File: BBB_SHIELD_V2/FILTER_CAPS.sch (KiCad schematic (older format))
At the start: 4 parts

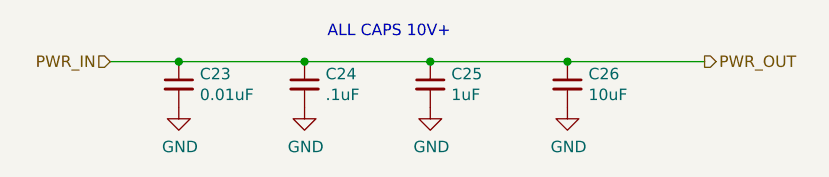
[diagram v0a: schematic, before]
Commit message: Changed to high-side switching of power supply to boards.  Changed footprints to SOIC.  Misc other changes.
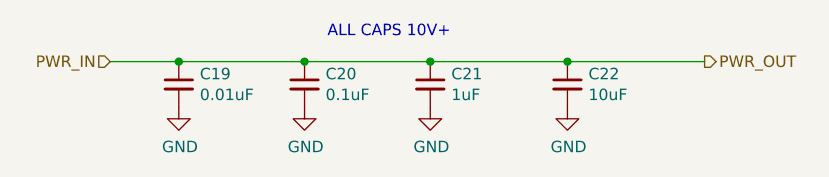
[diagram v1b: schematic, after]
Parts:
- C10: renamed from C18; DKPN (none) -> 1276-1052-1-ND; MFG (none) -> SAMSUNG; MFGPN (none) -> CL21A106KPFNNNE; NOTES (none) -> CT, VER 2018-12-09; TEMPCO (none) -> X5R; VOLTAGE (none) -> 10
- C7: renamed from C15; DKPN (none) -> 1276-1015-1-ND; MFG (none) -> SAMSUNG; MFGPN (none) -> CL21B103KBANNNC; NOTES (none) -> CT, VER 2018-11-25; TEMPCO (none) -> X7R; VOLTAGE (none) -> 50
- C8: renamed from C16; value .1uF -> 0.1uF; DKPN (none) -> 1276-1003-1-ND; MFG (none) -> SAMSUNG; MFGPN (none) -> CL21B104KBCNNNC; NOTES (none) -> REEL, VER 2018-11-25; TEMPCO (none) -> X7R; VOLTAGE (none) -> 50
- C9: renamed from C17; DKPN (none) -> 1276-2928-2-ND; MFG (none) -> SAMSUNG; MFGPN (none) -> CL21B105KBFNFNE; NOTES (none) -> REEL, VER 2018-11-25; TEMPCO (none) -> X7R; VOLTAGE (none) -> 50
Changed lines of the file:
@@
 $Descr A4 11693 8268
 encoding utf-8
-Sheet 7 11
+Sheet 9 12
 Title ""
 Date ""
@@
 PWR_OUT
 $Comp
-L Device:C_Small C15
+L Device:C_Small C7
 U 1 1 5B9ED5AB
 P 3400 2350
-AR Path="/5B9EA430/5B9ED537/5B9ED5AB" Ref="C15"  Part="1"
-AR Path="/5B9EA430/5B9F0FF8/5B9ED5AB" Ref="C19"  Part="1"
-AR Path="/5BA13116/5BD6D0DF/5B9ED5AB" Ref="C23"  Part="1"
-F 0 "C23" H 3492 2396 50  0000 L CNN
+AR Path="/5B9EA430/5B9ED537/5B9ED5AB" Ref="C7"  Part="1"
+AR Path="/5B9EA430/5B9F0FF8/5B9ED5AB" Ref="C11"  Part="1"
+AR Path="/5BA13116/5BD6D0DF/5B9ED5AB" Ref="C?"  Part="1"
+AR Path="/5BA13116/5D116931/5B9ED5AB" Ref="C15"  Part="1"
+AR Path="/5BA13116/5D1169A0/5B9ED5AB" Ref="C19"  Part="1"
+F 0 "C19" H 3492 2396 50  0000 L CNN
 F 1 "0.01uF" H 3492 2305 50  0000 L CNN
 F 2 "Capacitor_SMD:C_0805_2012Metric" H 3400 2350 50  0001 C CNN
-F 3 "~" H 3400 2350 50  0001 C CNN
+F 3 "" H 3400 2350 50  0001 C CNN
+F 4 "1276-1015-1-ND " H 0   0   50  0001 C CNN "DKPN"
+F 5 "SAMSUNG" H 0   0   50  0001 C CNN "MFG"
+F 6 "CL21B103KBANNNC" H 0   0   50  0001 C CNN "MFGPN"
+F 7 "CT, VER 2018-11-25" H 0   0   50  0001 C CNN "NOTES"
+F 8 "X7R" H 0   0   50  0001 C CNN "TEMPCO"
+F 9 "50" H 0   0   50  0001 C CNN "VOLTAGE"
 	1    3400 2350
 	1    0    0    -1
 $EndComp
 $Comp
-L Device:C_Small C16
+L Device:C_Small C8
 U 1 1 5B9ED653
 P 3950 2350
-AR Path="/5B9EA430/5B9ED537/5B9ED653" Ref="C16"  Part="1"
-AR Path="/5B9EA430/5B9F0FF8/5B9ED653" Ref="C20"  Part="1"
-AR Path="/5BA13116/5BD6D0DF/5B9ED653" Ref="C24"  Part="1"
-F 0 "C24" H 4042 2396 50  0000 L CNN
-F 1 ".1uF" H 4042 2305 50  0000 L CNN
+AR Path="/5B9EA430/5B9ED537/5B9ED653" Ref="C8"  Part="1"
+AR Path="/5B9EA430/5B9F0FF8/5B9ED653" Ref="C12"  Part="1"
+AR Path="/5BA13116/5BD6D0DF/5B9ED653" Ref="C?"  Part="1"
+AR Path="/5BA13116/5D116931/5B9ED653" Ref="C16"  Part="1"
+AR Path="/5BA13116/5D1169A0/5B9ED653" Ref="C20"  Part="1"
+F 0 "C20" H 4042 2396 50  0000 L CNN
+F 1 "0.1uF" H 4042 2305 50  0000 L CNN
 F 2 "Capacitor_SMD:C_0805_2012Metric" H 3950 2350 50  0001 C CNN
-F 3 "~" H 3950 2350 50  0001 C CNN
+F 3 "" H 3950 2350 50  0001 C CNN
+F 4 "1276-1003-1-ND " H 0   0   50  0001 C CNN "DKPN"
+F 5 "SAMSUNG" H 0   0   50  0001 C CNN "MFG"
+F 6 "CL21B104KBCNNNC" H 0   0   50  0001 C CNN "MFGPN"
+F 7 "X7R" H 0   0   50  0001 C CNN "TEMPCO"
+F 8 "50" H 0   0   50  0001 C CNN "VOLTAGE"
+F 9 "REEL, VER 2018-11-25" H 0   0   50  0001 C CNN "NOTES"
 	1    3950 2350
 	1    0    0    -1
 $EndComp
 $Comp
-L Device:C_Small C17
+L Device:C_Small C9
 U 1 1 5B9ED6C9
 P 4500 2350
-AR Path="/5B9EA430/5B9ED537/5B9ED6C9" Ref="C17"  Part="1"
-AR Path="/5B9EA430/5B9F0FF8/5B9ED6C9" Ref="C21"  Part="1"
-AR Path="/5BA13116/5BD6D0DF/5B9ED6C9" Ref="C25"  Part="1"
-F 0 "C25" H 4592 2396 50  0000 L CNN
+AR Path="/5B9EA430/5B9ED537/5B9ED6C9" Ref="C9"  Part="1"
+AR Path="/5B9EA430/5B9F0FF8/5B9ED6C9" Ref="C13"  Part="1"
+AR Path="/5BA13116/5BD6D0DF/5B9ED6C9" Ref="C?"  Part="1"
+AR Path="/5BA13116/5D116931/5B9ED6C9" Ref="C17"  Part="1"
+AR Path="/5BA13116/5D1169A0/5B9ED6C9" Ref="C21"  Part="1"
+F 0 "C21" H 4592 2396 50  0000 L CNN
 F 1 "1uF" H 4592 2305 50  0000 L CNN
 F 2 "Capacitor_SMD:C_0805_2012Metric" H 4500 2350 50  0001 C CNN
-F 3 "~" H 4500 2350 50  0001 C CNN
+F 3 "" H 4500 2350 50  0001 C CNN
+F 4 " 1276-2928-2-ND " H 0   0   50  0001 C CNN "DKPN"
+F 5 "SAMSUNG" H 0   0   50  0001 C CNN "MFG"
+F 6 "CL21B105KBFNFNE" H 0   0   50  0001 C CNN "MFGPN"
+F 7 "X7R" H 0   0   50  0001 C CNN "TEMPCO"
+F 8 "50" H 0   0   50  0001 C CNN "VOLTAGE"
+F 9 "REEL, VER 2018-11-25" H 0   0   50  0001 C CNN "NOTES"
 	1    4500 2350
 	1    0    0    -1
 $EndComp
 $Comp
-L Device:C_Small C18
+L Device:C_Small C10
 U 1 1 5B9ED7ED
 P 5100 2350
-AR Path="/5B9EA430/5B9ED537/5B9ED7ED" Ref="C18"  Part="1"
-AR Path="/5B9EA430/5B9F0FF8/5B9ED7ED" Ref="C22"  Part="1"
-AR Path="/5BA13116/5BD6D0DF/5B9ED7ED" Ref="C26"  Part="1"
-F 0 "C26" H 5192 2396 50  0000 L CNN
+AR Path="/5B9EA430/5B9ED537/5B9ED7ED" Ref="C10"  Part="1"
+AR Path="/5B9EA430/5B9F0FF8/5B9ED7ED" Ref="C14"  Part="1"
+AR Path="/5BA13116/5BD6D0DF/5B9ED7ED" Ref="C?"  Part="1"
+AR Path="/5BA13116/5D116931/5B9ED7ED" Ref="C18"  Part="1"
+AR Path="/5BA13116/5D1169A0/5B9ED7ED" Ref="C22"  Part="1"
+F 0 "C22" H 5192 2396 50  0000 L CNN
 F 1 "10uF" H 5192 2305 50  0000 L CNN
 F 2 "Capacitor_SMD:C_0805_2012Metric" H 5100 2350 50  0001 C CNN
-F 3 "~" H 5100 2350 50  0001 C CNN
+F 3 "" H 5100 2350 50  0001 C CNN
+F 4 "CT, VER 2018-12-09" H 0   0   50  0001 C CNN "NOTES"
+F 5 "1276-1052-1-ND" H 0   0   50  0001 C CNN "DKPN"
+F 6 "SAMSUNG" H 0   0   50  0001 C CNN "MFG"
+F 7 "CL21A106KPFNNNE" H 0   0   50  0001 C CNN "MFGPN"
+F 8 "X5R" H 0   0   50  0001 C CNN "TEMPCO"
+F 9 "10" H 0   0   50  0001 C CNN "VOLTAGE"
 	1    5100 2350
 	1    0    0    -1
@@
 	5100 2250 5700 2250
 $Comp
-L power:GND #PWR020
+L power:GND #PWR015
 U 1 1 5B9F0E38
 P 3400 2450
-AR Path="/5B9EA430/5B9ED537/5B9F0E38" Ref="#PWR020"  Part="1"
-AR Path="/5B9EA430/5B9F0FF8/5B9F0E38" Ref="#PWR024"  Part="1"
-AR Path="/5BA13116/5BD6D0DF/5B9F0E38" Ref="#PWR043"  Part="1"
+AR Path="/5B9EA430/5B9ED537/5B9F0E38" Ref="#PWR015"  Part="1"
+AR Path="/5B9EA430/5B9F0FF8/5B9F0E38" Ref="#PWR019"  Part="1"
+AR Path="/5BA13116/5BD6D0DF/5B9F0E38" Ref="#PWR?"  Part="1"
+AR Path="/5BA13116/5D116931/5B9F0E38" Ref="#PWR039"  Part="1"
+AR Path="/5BA13116/5D1169A0/5B9F0E38" Ref="#PWR043"  Part="1"
 F 0 "#PWR043" H 3400 2200 50  0001 C CNN
 F 1 "GND" H 3405 2277 50  0000 C CNN
@@
 $EndComp
 $Comp
-L power:GND #PWR021
+L power:GND #PWR016
 U 1 1 5B9F0E52
 P 3950 2450
-AR Path="/5B9EA430/5B9ED537/5B9F0E52" Ref="#PWR021"  Part="1"
-AR Path="/5B9EA430/5B9F0FF8/5B9F0E52" Ref="#PWR025"  Part="1"
-AR Path="/5BA13116/5BD6D0DF/5B9F0E52" Ref="#PWR044"  Part="1"
+AR Path="/5B9EA430/5B9ED537/5B9F0E52" Ref="#PWR016"  Part="1"
+AR Path="/5B9EA430/5B9F0FF8/5B9F0E52" Ref="#PWR020"  Part="1"
+AR Path="/5BA13116/5BD6D0DF/5B9F0E52" Ref="#PWR?"  Part="1"
+AR Path="/5BA13116/5D116931/5B9F0E52" Ref="#PWR040"  Part="1"
+AR Path="/5BA13116/5D1169A0/5B9F0E52" Ref="#PWR044"  Part="1"
 F 0 "#PWR044" H 3950 2200 50  0001 C CNN
 F 1 "GND" H 3955 2277 50  0000 C CNN
@@
 $EndComp
 $Comp
-L power:GND #PWR022
+L power:GND #PWR017
 U 1 1 5B9F0E65
 P 4500 2450
-AR Path="/5B9EA430/5B9ED537/5B9F0E65" Ref="#PWR022"  Part="1"
-AR Path="/5B9EA430/5B9F0FF8/5B9F0E65" Ref="#PWR026"  Part="1"
-AR Path="/5BA13116/5BD6D0DF/5B9F0E65" Ref="#PWR045"  Part="1"
+AR Path="/5B9EA430/5B9ED537/5B9F0E65" Ref="#PWR017"  Part="1"
+AR Path="/5B9EA430/5B9F0FF8/5B9F0E65" Ref="#PWR021"  Part="1"
+AR Path="/5BA13116/5BD6D0DF/5B9F0E65" Ref="#PWR?"  Part="1"
+AR Path="/5BA13116/5D116931/5B9F0E65" Ref="#PWR041"  Part="1"
+AR Path="/5BA13116/5D1169A0/5B9F0E65" Ref="#PWR045"  Part="1"
 F 0 "#PWR045" H 4500 2200 50  0001 C CNN
 F 1 "GND" H 4505 2277 50  0000 C CNN
@@
 $EndComp
 $Comp
-L power:GND #PWR023
+L power:GND #PWR018
 U 1 1 5B9F0E78
 P 5100 2450
-AR Path="/5B9EA430/5B9ED537/5B9F0E78" Ref="#PWR023"  Part="1"
-AR Path="/5B9EA430/5B9F0FF8/5B9F0E78" Ref="#PWR027"  Part="1"
-AR Path="/5BA13116/5BD6D0DF/5B9F0E78" Ref="#PWR046"  Part="1"
+AR Path="/5B9EA430/5B9ED537/5B9F0E78" Ref="#PWR018"  Part="1"
+AR Path="/5B9EA430/5B9F0FF8/5B9F0E78" Ref="#PWR022"  Part="1"
+AR Path="/5BA13116/5BD6D0DF/5B9F0E78" Ref="#PWR?"  Part="1"
+AR Path="/5BA13116/5D116931/5B9F0E78" Ref="#PWR042"  Part="1"
+AR Path="/5BA13116/5D1169A0/5B9F0E78" Ref="#PWR046"  Part="1"
 F 0 "#PWR046" H 5100 2200 50  0001 C CNN
 F 1 "GND" H 5105 2277 50  0000 C CNN

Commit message: Rev 2 problem fixes.
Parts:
- C10: NOTES CT, VER 2018-12-09 -> VER,2019-07-17,CT
- C7: NOTES CT, VER 2018-11-25 -> VER,2019-07-17,CT
- C8, C9: NOTES REEL, VER 2018-11-25 -> VER,2019-07-17,REEL
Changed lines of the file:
@@
 AR Path="/5BA13116/5D116931/5B9ED5AB" Ref="C15"  Part="1"
 AR Path="/5BA13116/5D1169A0/5B9ED5AB" Ref="C19"  Part="1"
-F 0 "C19" H 3492 2396 50  0000 L CNN
+F 0 "C15" H 3492 2396 50  0000 L CNN
 F 1 "0.01uF" H 3492 2305 50  0000 L CNN
 F 2 "Capacitor_SMD:C_0805_2012Metric" H 3400 2350 50  0001 C CNN
@@
 F 5 "SAMSUNG" H 0   0   50  0001 C CNN "MFG"
 F 6 "CL21B103KBANNNC" H 0   0   50  0001 C CNN "MFGPN"
-F 7 "CT, VER 2018-11-25" H 0   0   50  0001 C CNN "NOTES"
+F 7 "VER,2019-07-17,CT" H 0   0   50  0001 C CNN "NOTES"
 F 8 "X7R" H 0   0   50  0001 C CNN "TEMPCO"
 F 9 "50" H 0   0   50  0001 C CNN "VOLTAGE"
@@
 AR Path="/5BA13116/5D116931/5B9ED653" Ref="C16"  Part="1"
 AR Path="/5BA13116/5D1169A0/5B9ED653" Ref="C20"  Part="1"
-F 0 "C20" H 4042 2396 50  0000 L CNN
+F 0 "C16" H 4042 2396 50  0000 L CNN
 F 1 "0.1uF" H 4042 2305 50  0000 L CNN
 F 2 "Capacitor_SMD:C_0805_2012Metric" H 3950 2350 50  0001 C CNN
@@
 F 7 "X7R" H 0   0   50  0001 C CNN "TEMPCO"
 F 8 "50" H 0   0   50  0001 C CNN "VOLTAGE"
-F 9 "REEL, VER 2018-11-25" H 0   0   50  0001 C CNN "NOTES"
+F 9 "VER,2019-07-17,REEL" H 0   0   50  0001 C CNN "NOTES"
 	1    3950 2350
 	1    0    0    -1
@@
 AR Path="/5BA13116/5D116931/5B9ED6C9" Ref="C17"  Part="1"
 AR Path="/5BA13116/5D1169A0/5B9ED6C9" Ref="C21"  Part="1"
-F 0 "C21" H 4592 2396 50  0000 L CNN
+F 0 "C17" H 4592 2396 50  0000 L CNN
 F 1 "1uF" H 4592 2305 50  0000 L CNN
 F 2 "Capacitor_SMD:C_0805_2012Metric" H 4500 2350 50  0001 C CNN
@@
 F 7 "X7R" H 0   0   50  0001 C CNN "TEMPCO"
 F 8 "50" H 0   0   50  0001 C CNN "VOLTAGE"
-F 9 "REEL, VER 2018-11-25" H 0   0   50  0001 C CNN "NOTES"
+F 9 "VER,2019-07-17,REEL" H 0   0   50  0001 C CNN "NOTES"
 	1    4500 2350
 	1    0    0    -1
@@
 AR Path="/5BA13116/5D116931/5B9ED7ED" Ref="C18"  Part="1"
 AR Path="/5BA13116/5D1169A0/5B9ED7ED" Ref="C22"  Part="1"
-F 0 "C22" H 5192 2396 50  0000 L CNN
+F 0 "C18" H 5192 2396 50  0000 L CNN
 F 1 "10uF" H 5192 2305 50  0000 L CNN
 F 2 "Capacitor_SMD:C_0805_2012Metric" H 5100 2350 50  0001 C CNN
 F 3 "" H 5100 2350 50  0001 C CNN
-F 4 "CT, VER 2018-12-09" H 0   0   50  0001 C CNN "NOTES"
+F 4 "VER,2019-07-17,CT" H 0   0   50  0001 C CNN "NOTES"
 F 5 "1276-1052-1-ND" H 0   0   50  0001 C CNN "DKPN"
 F 6 "SAMSUNG" H 0   0   50  0001 C CNN "MFG"
@@
 AR Path="/5BA13116/5D116931/5B9F0E38" Ref="#PWR039"  Part="1"
 AR Path="/5BA13116/5D1169A0/5B9F0E38" Ref="#PWR043"  Part="1"
-F 0 "#PWR043" H 3400 2200 50  0001 C CNN
+F 0 "#PWR039" H 3400 2200 50  0001 C CNN
 F 1 "GND" H 3405 2277 50  0000 C CNN
 F 2 "" H 3400 2450 50  0001 C CNN
@@
 AR Path="/5BA13116/5D116931/5B9F0E52" Ref="#PWR040"  Part="1"
 AR Path="/5BA13116/5D1169A0/5B9F0E52" Ref="#PWR044"  Part="1"
-F 0 "#PWR044" H 3950 2200 50  0001 C CNN
+F 0 "#PWR040" H 3950 2200 50  0001 C CNN
 F 1 "GND" H 3955 2277 50  0000 C CNN
 F 2 "" H 3950 2450 50  0001 C CNN
@@
 AR Path="/5BA13116/5D116931/5B9F0E65" Ref="#PWR041"  Part="1"
 AR Path="/5BA13116/5D1169A0/5B9F0E65" Ref="#PWR045"  Part="1"
-F 0 "#PWR045" H 4500 2200 50  0001 C CNN
+F 0 "#PWR041" H 4500 2200 50  0001 C CNN
 F 1 "GND" H 4505 2277 50  0000 C CNN
 F 2 "" H 4500 2450 50  0001 C CNN
@@
 AR Path="/5BA13116/5D116931/5B9F0E78" Ref="#PWR042"  Part="1"
 AR Path="/5BA13116/5D1169A0/5B9F0E78" Ref="#PWR046"  Part="1"
-F 0 "#PWR046" H 5100 2200 50  0001 C CNN
+F 0 "#PWR042" H 5100 2200 50  0001 C CNN
 F 1 "GND" H 5105 2277 50  0000 C CNN
 F 2 "" H 5100 2450 50  0001 C CNN
